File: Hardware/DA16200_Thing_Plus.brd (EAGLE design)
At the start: 22.9 x 59.7 mm, 131 parts, among them J2 THING_PLUS, J3 Qwiic, J5 USB C, J7 CORTEX_JTAG_DEBUG_PTH_NS, Q1 20V/4.2A/52mΩ/1.4W, U1 DA16200MOD, U2 CH340E_MSOP10, U3 MCP73831, U7 XC6222B331MR-G

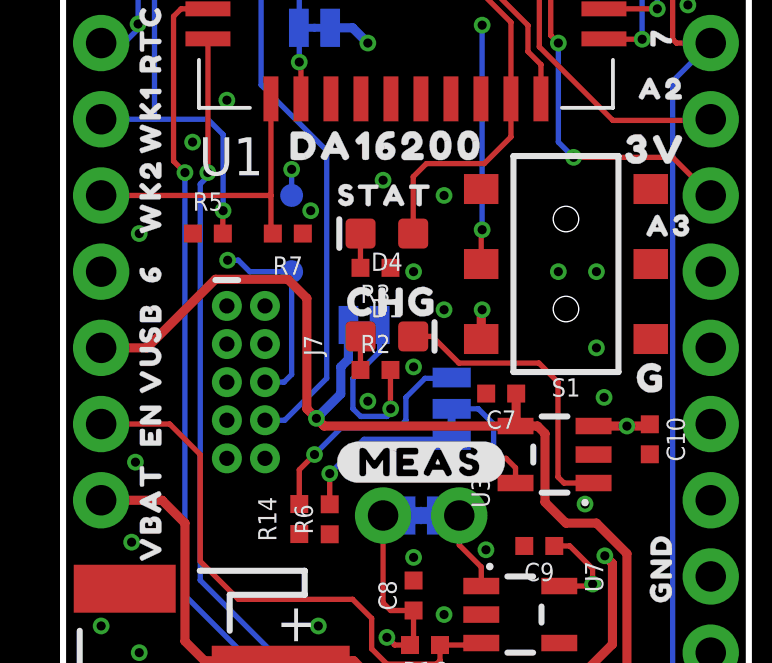
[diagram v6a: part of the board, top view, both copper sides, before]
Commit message: Update back buzzard labels
Pin labels should be rounded and call out GPIO it's connected to
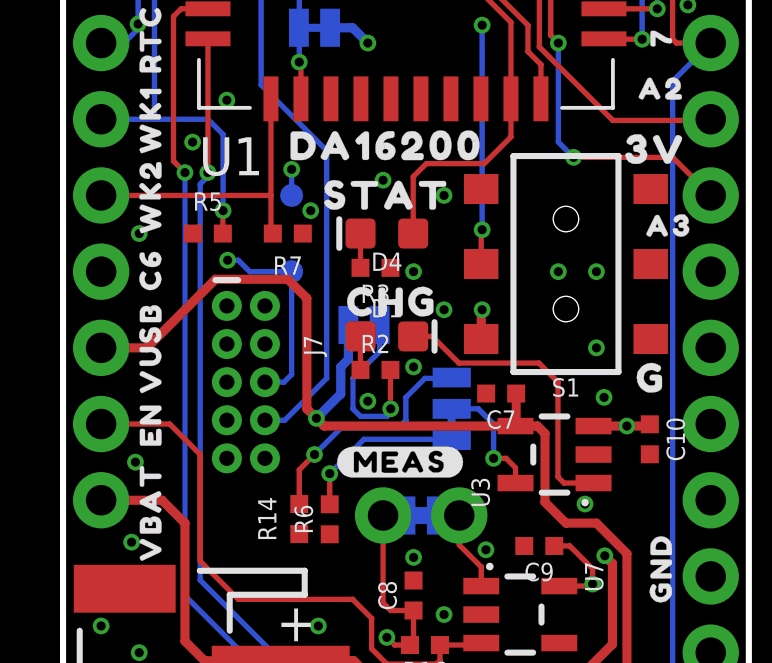
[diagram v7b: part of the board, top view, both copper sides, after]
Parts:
- removed U$30: (no value), output:#POCI#0
- removed U$43: (no value), output:#PICO#0
- removed U$46: (no value), output:#SCLK#0
- removed U$48: (no value), output:#A2#0
- removed U$49: (no value), output:#A3#0
- removed U$61: (no value), output:#DA_MEAS#0
- removed U$76: (no value), output:##CSB##0
- removed U$77: (no value), output:#SCL#0
- removed U$78: (no value), output:#SDA#0
- added U$11: (no value), output:#0#SDA#0
- added U$12: (no value), output:#1#SCL#0
- added U$62: (no value), output:#6##CSB##0
- added U$63: (no value), output:#11#LED#0
- added U$65: (no value), output:C60
- added U$66: (no value), output:#9#POCI#0
- added U$67: (no value), output:#8#PICO#0
- added U$68: (no value), output:#7#SCLK#0
- added U$69: (no value), output:#2#A2#0
- added U$70: (no value), output:#3#A3#0
- U$17: device output:#TXO#0 -> output:#DA#0
- U$27: device output:#IO10#0 -> output:#4#TXO#0
- U$29: device output:#RXI#0 -> output:#MEAS#0
- U$36: device output:60 -> output:#5#RXI#0
- U$7: device output:#LED_#0 -> output:#IOA10#0
- moved U$36 24.4 mm to (21.2, 47.0), flipped to the bottom, turned to 0 degrees
- moved U$27 15.9 mm to (21.2, 49.5)
- moved U$17 12.1 mm to (13.2, 40.5)
- moved U$29 10.5 mm to (14.1, 39.2)
- moved U$7 2.96 mm to (7.24, 44.5)
- moved U$1 0.63 mm to (8.00, 34.3)
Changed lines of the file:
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@@
 <?xml version="1.0" encoding="utf-8"?>
 <!DOCTYPE eagle SYSTEM "eagle.dtd">
-<eagle version="9.5.2">
+<eagle version="9.4.2">
 <drawing>
 <settings>
@@
 <layers>
 <layer number="1" name="Top" color="4" fill="1" visible="yes" active="yes"/>
-<layer number="2" name="gndvert" color="10" fill="7" visible="yes" active="yes"/>
-<layer number="15" name="pwrhorz" color="4" fill="7" visible="yes" active="yes"/>
+<layer number="2" name="gndvert" color="10" fill="7" visible="no" active="yes"/>
+<layer number="15" name="pwrhorz" color="4" fill="7" visible="no" active="yes"/>
 <layer number="16" name="Bottom" color="1" fill="1" visible="yes" active="yes"/>
 <layer number="17" name="Pads" color="2" fill="1" visible="yes" active="yes"/>
@@
 <layer number="37" name="tTest" color="7" fill="1" visible="no" active="yes"/>
 <layer number="38" name="bTest" color="7" fill="1" visible="no" active="yes"/>
-<layer number="39" name="tKeepout" color="4" fill="11" visible="yes" active="yes"/>
+<layer number="39" name="tKeepout" color="4" fill="11" visible="no" active="yes"/>
 <layer number="40" name="bKeepout" color="1" fill="11" visible="no" active="yes"/>
 <layer number="41" name="tRestrict" color="4" fill="10" visible="no" active="yes"/>
@@
 <layer number="45" name="Holes" color="7" fill="1" visible="yes" active="yes"/>
 <layer number="46" name="Milling" color="3" fill="1" visible="no" active="yes"/>
-<layer number="47" name="Measures" color="7" fill="1" visible="yes" active="yes"/>
+<layer number="47" name="Measures" color="7" fill="1" visible="no" active="yes"/>
 <layer number="48" name="Document" color="7" fill="1" visible="no" active="yes"/>
 <layer number="49" name="Reference" color="7" fill="1" visible="no" active="yes"/>
@@
 <element name="LOGO1" library="SparkFun-Aesthetics" package="OSHW-LOGO-S" value="OSHW-LOGOS" x="2.54" y="5.715" smashed="yes" rot="MR0"/>
 <element name="LOGO2" library="SparkFun-Aesthetics" package="SFE_LOGO_NAME_FLAME_.1" value="SFE_LOGO_NAME_FLAME.1_INCH" x="11.303" y="54.356" smashed="yes" rot="MR0"/>
-<element name="U$17" library="output" package="#TXO#0" value="" x="21.209" y="49.53" smashed="yes" rot="MR0"/>
-<element name="U$29" library="output" package="#RXI#0" value="" x="21.209" y="46.99" smashed="yes" rot="MR0"/>
-<element name="U$30" library="output" package="#POCI#0" value="" x="21.209" y="44.45" smashed="yes" rot="MR0"/>
-<element name="U$43" library="output" package="#PICO#0" value="" x="21.209" y="41.91" smashed="yes" rot="MR0"/>
-<element name="U$46" library="output" package="#SCLK#0" value="" x="21.209" y="39.37" smashed="yes" rot="MR0"/>
-<element name="U$48" library="output" package="#A2#0" value="" x="21.209" y="36.83" smashed="yes" rot="MR0"/>
-<element name="U$49" library="output" package="#A3#0" value="" x="21.209" y="34.29" smashed="yes" rot="MR0"/>
 <element name="U$50" library="output" package="#GND#0" value="" x="21.209" y="21.59" smashed="yes" rot="MR0"/>
 <element name="U$51" library="output" package="#3V3#0" value="" x="21.209" y="16.51" smashed="yes" rot="MR0"/>
@@
 <element name="U$72" library="output" package="#WK1#0" value="" x="5.969" y="36.83" smashed="yes" rot="MR0"/>
 <element name="U$73" library="output" package="#RTC#0" value="" x="5.969" y="39.37" smashed="yes" rot="MR0"/>
-<element name="U$76" library="output" package="##CSB##0" value="" x="5.842" y="46.99" smashed="yes" rot="MR0"/>
-<element name="U$77" library="output" package="#SCL#0" value="" x="5.715" y="49.53" smashed="yes" rot="MR0"/>
-<element name="U$78" library="output" package="#SDA#0" value="" x="5.969" y="52.07" smashed="yes" rot="MR0"/>
 <element name="U$79" library="output" package="#VBT#0" value="" x="6.096" y="24.13" smashed="yes" rot="MR0"/>
 <element name="U$56" library="output" package="THING_PLUS0" value="" x="16.256" y="34.544" smashed="yes" rot="MR0"/>
@@
 <element name="U$84" library="output" package="#LED#0" value="" x="18.288" y="7.239" smashed="yes" rot="MR0"/>
 <element name="U$85" library="output" package="#SHLD#0" value="" x="13.208" y="2.921" smashed="yes" rot="MR0"/>
-<element name="U$1" library="output" package="STAT0" value="" x="8.636" y="34.29" smashed="yes"/>
+<element name="U$1" library="output" package="STAT0" value="" x="8.001" y="34.29" smashed="yes"/>
 <element name="U$2" library="output" package="CHG0" value="" x="8.763" y="30.734" smashed="yes"/>
 <element name="U$5" library="output" package="##RST##0" value="" x="21.209" y="13.97" smashed="yes" rot="MR0"/>
@@
 <element name="TMS" library="SparkFun-Connectors" package="PAD.03X.03" value="TEST-POINT3" x="7.62" y="34.29" smashed="yes" rot="MR0"/>
 <element name="GPIOC7" library="SparkFun-Connectors" package="PAD.03X.03" value="TEST-POINT3" x="7.62" y="31.75" smashed="yes" rot="MR0"/>
-<element name="U$7" library="output" package="#LED_#0" value="" x="5.715" y="41.91" smashed="yes" rot="MR0"/>
 <element name="U$8" library="output" package="#MEAS#0" value="" x="9.144" y="25.4" smashed="yes"/>
 <element name="U$3" library="output" package="#MEAS_#0" value="" x="17.907" y="23.622" smashed="yes" rot="MR0"/>
@@
 <element name="U$25" library="output" package="SCL0" value="" x="2.921" y="47.879" smashed="yes" rot="R90"/>
 <element name="U$26" library="output" package="#CSB#0" value="" x="2.794" y="45.212" smashed="yes" rot="R90"/>
-<element name="U$27" library="output" package="#IO10#0" value="" x="6.096" y="44.45" smashed="yes" rot="MR0"/>
 <element name="U$32" library="output" package="100" value="" x="2.921" y="43.307" smashed="yes" rot="R90"/>
 <element name="U$33" library="output" package="RTC0" value="" x="2.921" y="37.846" smashed="yes" rot="R90"/>
 <element name="U$34" library="output" package="WK10" value="" x="2.921" y="35.179" smashed="yes" rot="R90"/>
 <element name="U$35" library="output" package="WK20" value="" x="2.921" y="32.512" smashed="yes" rot="R90"/>
-<element name="U$36" library="output" package="60" value="" x="2.921" y="30.861" smashed="yes" rot="R90"/>
 <element name="U$37" library="output" package="EN0" value="" x="2.921" y="25.4" smashed="yes" rot="R90"/>
 <element name="U$38" library="output" package="VUSB0" value="" x="2.921" y="27.178" smashed="yes" rot="R90"/>
@@
 <element name="U$58" library="output" package="70" value="" x="19.685" y="14.859" smashed="yes"/>
 <element name="U$59" library="output" package="#CHG#0" value="" x="15.24" y="29.845" smashed="yes" rot="MR0"/>
-<element name="U$61" library="output" package="#DA_MEAS#0" value="" x="16.002" y="39.751" smashed="yes" rot="MR0"/>
 <element name="U$10" library="output" package="#CH340#0" value="" x="20.701" y="11.43" smashed="yes" rot="MR0"/>
+<element name="U$11" library="output" package="#0#SDA#0" value="" x="7.747" y="52.07" smashed="yes" rot="MR0"/>
+<element name="U$12" library="output" package="#1#SCL#0" value="" x="7.239" y="49.53" smashed="yes" rot="MR0"/>
+<element name="U$62" library="output" package="#6##CSB##0" value="" x="7.493" y="46.99" smashed="yes" rot="MR0"/>
+<element name="U$63" library="output" package="#11#LED#0" value="" x="8.001" y="41.91" smashed="yes" rot="MR0"/>
+<element name="U$65" library="output" package="C60" value="" x="2.921" y="30.607" smashed="yes" rot="R90"/>
+<element name="U$7" library="output" package="#IOA10#0" value="" x="7.239" y="44.45" smashed="yes" rot="MR0"/>
+<element name="U$27" library="output" package="#4#TXO#0" value="" x="21.209" y="49.53" smashed="yes" rot="MR0"/>
+<element name="U$36" library="output" package="#5#RXI#0" value="" x="21.209" y="46.99" smashed="yes" rot="MR0"/>
+<element name="U$66" library="output" package="#9#POCI#0" value="" x="21.209" y="44.45" smashed="yes" rot="MR0"/>
+<element name="U$67" library="output" package="#8#PICO#0" value="" x="21.209" y="41.91" smashed="yes" rot="MR0"/>
+<element name="U$68" library="output" package="#7#SCLK#0" value="" x="21.336" y="39.37" smashed="yes" rot="MR0"/>
+<element name="U$69" library="output" package="#2#A2#0" value="" x="21.209" y="36.83" smashed="yes" rot="MR0"/>
+<element name="U$70" library="output" package="#3#A3#0" value="" x="21.209" y="34.29" smashed="yes" rot="MR0"/>
+<element name="U$17" library="output" package="#DA#0" value="" x="13.208" y="40.513" smashed="yes" rot="MR0"/>
+<element name="U$29" library="output" package="#MEAS#0" value="" x="14.097" y="39.243" smashed="yes" rot="MR0"/>
 </elements>
 <signals>

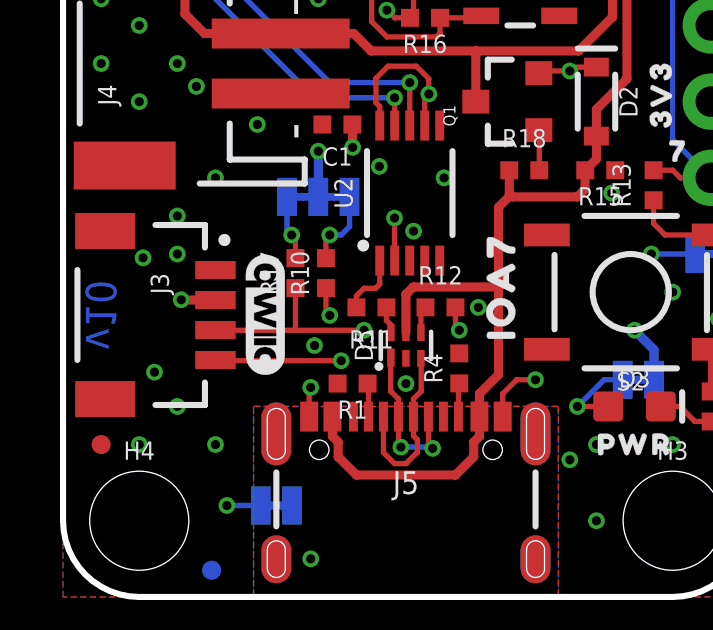
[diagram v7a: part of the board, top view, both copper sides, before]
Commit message: Panelize
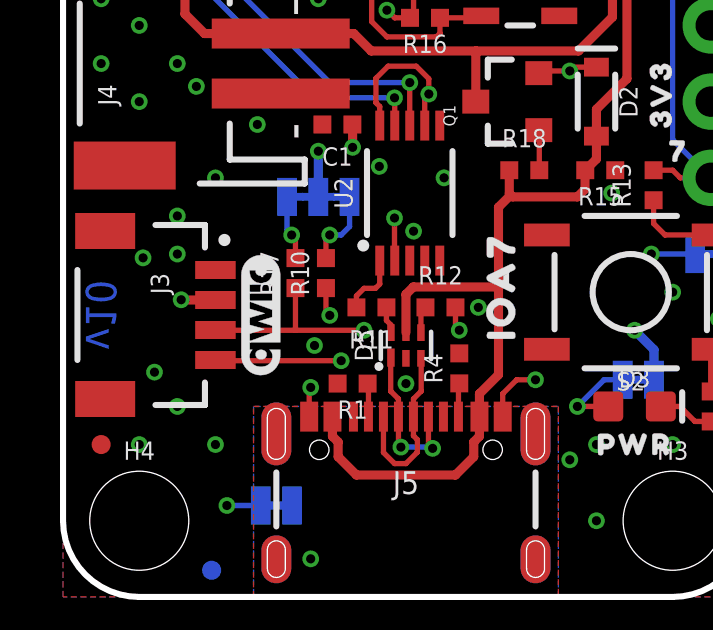
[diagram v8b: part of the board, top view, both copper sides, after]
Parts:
- removed U$79: (no value), output:#VBT#0
- added U$30: (no value), output:#VBAT#0
- moved U$64 0.13 mm to (6.60, 9.40), turned to 90 degrees
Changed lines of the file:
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@@
 <attribute name="VALUE" value="2.0K" x="9.452" y="23.495" size="0.6096" layer="27" font="vector" ratio="20" rot="R90" align="top-center"/>
 </element>
-<element name="U$64" library="SparkFun-Aesthetics" package="QWIIC_4MM" value="" x="6.731" y="9.398" smashed="yes" rot="R270"/>
+<element name="U$64" library="SparkFun-Aesthetics" package="QWIIC_4MM" value="" x="6.604" y="9.398" smashed="yes" rot="R90"/>
 <element name="R8" library="SparkFun-Resistors" package="0402-TIGHT" value="1k" x="21.59" y="6.35" smashed="yes" rot="R270">
 <attribute name="NAME" x="22.152" y="6.35" size="0.6096" layer="25" font="vector" ratio="20" rot="R270" align="bottom-center"/>
@@
 <element name="U$72" library="output" package="#WK1#0" value="" x="5.969" y="36.83" smashed="yes" rot="MR0"/>
 <element name="U$73" library="output" package="#RTC#0" value="" x="5.969" y="39.37" smashed="yes" rot="MR0"/>
-<element name="U$79" library="output" package="#VBT#0" value="" x="6.096" y="24.13" smashed="yes" rot="MR0"/>
 <element name="U$56" library="output" package="THING_PLUS0" value="" x="16.256" y="34.544" smashed="yes" rot="MR0"/>
 <element name="U$80" library="output" package="DA162000" value="" x="15.494" y="32.639" smashed="yes" rot="MR0"/>
@@
 <element name="U$17" library="output" package="#DA#0" value="" x="13.208" y="40.513" smashed="yes" rot="MR0"/>
 <element name="U$29" library="output" package="#MEAS#0" value="" x="14.097" y="39.243" smashed="yes" rot="MR0"/>
+<element name="U$30" library="output" package="#VBAT#0" value="" x="7.366" y="24.13" smashed="yes" rot="MR0"/>
 </elements>
 <signals>
